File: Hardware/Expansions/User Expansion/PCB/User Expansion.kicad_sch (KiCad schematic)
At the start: 44 parts, among them J101 10018784-10201TLF, U101 M24C02-FMN

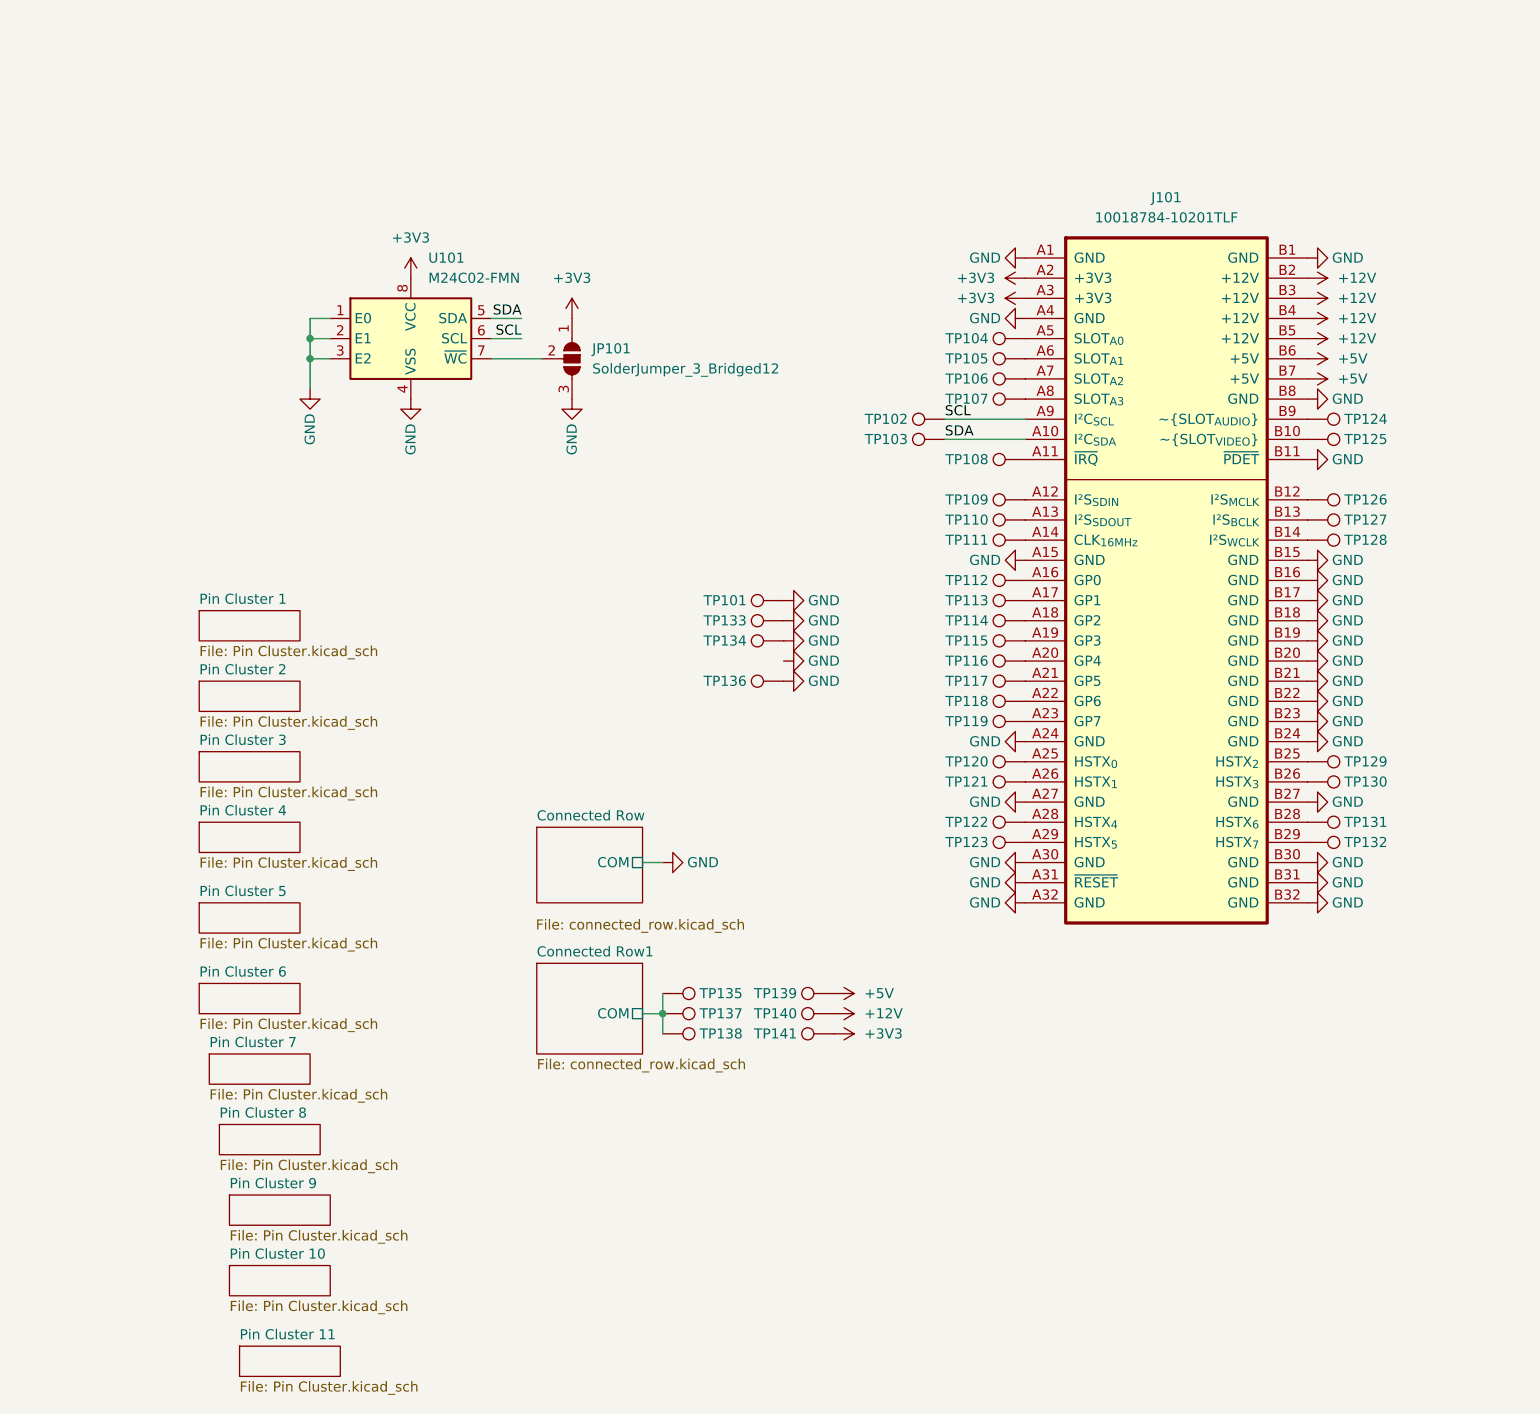
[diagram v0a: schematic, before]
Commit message: Overhauls user expansion and updates design to new platform decisions.
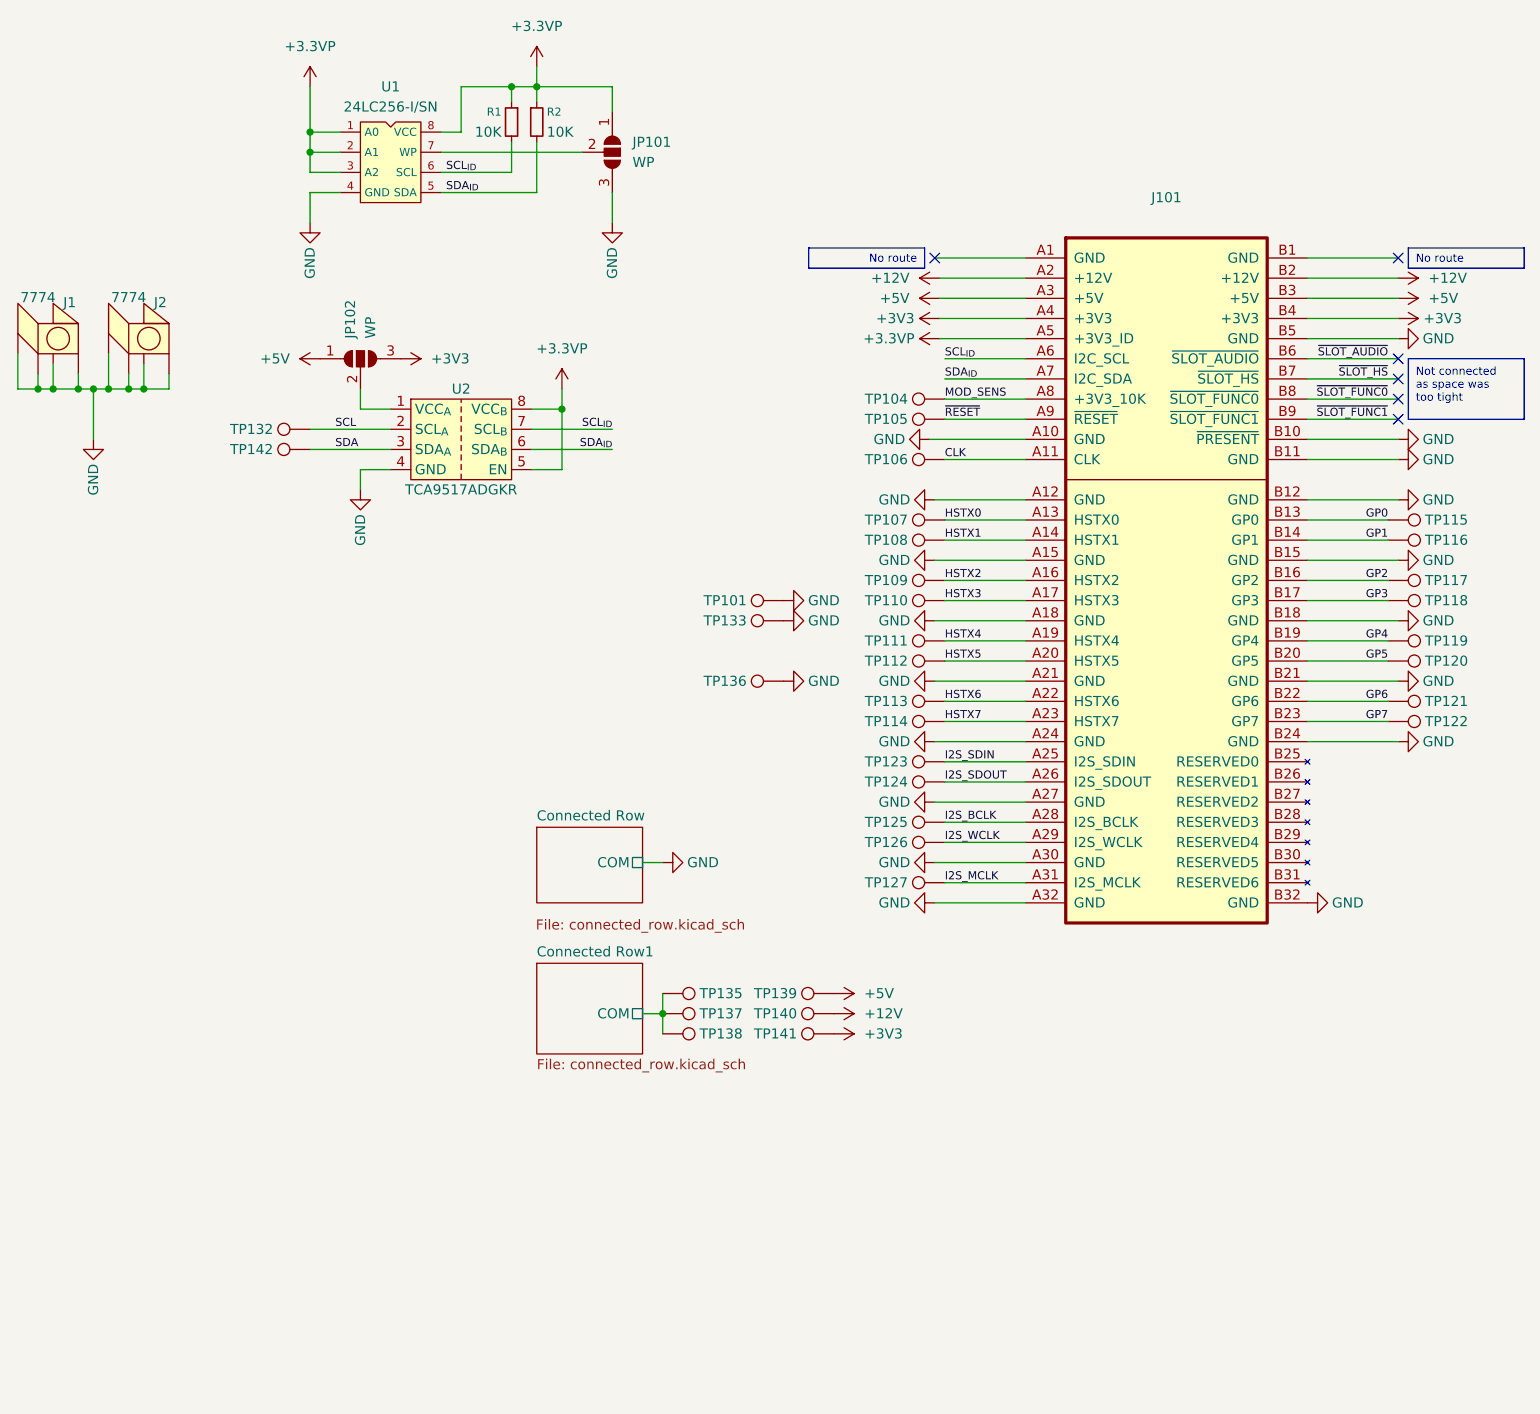
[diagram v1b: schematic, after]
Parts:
- removed TP102: SCL, TestPoint:TestPoint_THTPad_D1.5mm_Drill0.7mm, symbol Connector:TestPoint
- removed TP103: SDA, TestPoint:TestPoint_THTPad_D1.5mm_Drill0.7mm, symbol Connector:TestPoint
- removed TP128: WCLK, TestPoint:TestPoint_THTPad_D1.5mm_Drill0.7mm, symbol Connector:TestPoint
- removed TP129: HSTX2, TestPoint:TestPoint_THTPad_D1.5mm_Drill0.7mm, symbol Connector:TestPoint
- removed TP130: HSTX3, TestPoint:TestPoint_THTPad_D1.5mm_Drill0.7mm, symbol Connector:TestPoint
- removed TP131: HSTX6, TestPoint:TestPoint_THTPad_D1.5mm_Drill0.7mm, symbol Connector:TestPoint
- removed TP134: GP7, TestPoint:TestPoint_THTPad_D1.5mm_Drill0.7mm, symbol Connector:TestPoint
- removed U101: M24C02-FMN, Package_SO:SOIC-8_3.9x4.9mm_P1.27mm, symbol Memory_EEPROM:M24C02-FMN
- added J1, J2: 7774, Home Computer:KEYSTONE_7774, symbol Home Computer:7774
- added JP102: WP, Jumper:SolderJumper-3_P1.3mm_Open_RoundedPad1.0x1.5mm, symbol Jumper:SolderJumper_3_Open
- added R1, R2: 10K, Resistor_SMD:R_0805_2012Metric_Pad1.20x1.40mm_HandSolder, symbol Device:R_Small
- added TP142: (no value), Home Computer:Perfboard_Pad_P2.54mm, symbol Connector:TestPoint
- added U1: 24LC256-I/SN, Package_SO:SOIC-8_3.9x4.9mm_P1.27mm, symbol Home Computer:24LC256
- added U2: TCA9517ADGKR, Package_SO:VSSOP-8_3x3mm_P0.65mm, symbol Home Computer:TCA9517ADGKR
- J101: value 10018784-10201TLF -> (none); symbol Home Computer:AHC-MODCONN-GEN1 Socket -> Home Computer:AHC-CONN-EXP-CARD; MANUFACTURER AMPHENOL -> (none); PARTREV A -> (none); STANDARD MANUFACTURER RECOMMENDATIONS -> (none)
- JP101: value SolderJumper_3_Bridged12 -> WP
- TP101, TP119, TP133, TP135, TP136, TP137, TP138, TP139, TP140, TP141: value GP7 -> (none); footprint TestPoint:TestPoint_THTPad_D1.5mm_Drill0.7mm -> Home Computer:Perfboard_Pad_P2.54mm
- TP104: value A0 -> (none); footprint TestPoint:TestPoint_THTPad_D1.5mm_Drill0.7mm -> Home Computer:Perfboard_Pad_P2.54mm
- TP105: value A1 -> (none); footprint TestPoint:TestPoint_THTPad_D1.5mm_Drill0.7mm -> Home Computer:Perfboard_Pad_P2.54mm
- TP106: value A2 -> (none); footprint TestPoint:TestPoint_THTPad_D1.5mm_Drill0.7mm -> Home Computer:Perfboard_Pad_P2.54mm
- TP107: value A3 -> (none); footprint TestPoint:TestPoint_THTPad_D1.5mm_Drill0.7mm -> Home Computer:Perfboard_Pad_P2.54mm
- TP108: value IRQ -> (none); footprint TestPoint:TestPoint_THTPad_D1.5mm_Drill0.7mm -> Home Computer:Perfboard_Pad_P2.54mm
- TP109: value SDIN -> (none); footprint TestPoint:TestPoint_THTPad_D1.5mm_Drill0.7mm -> Home Computer:Perfboard_Pad_P2.54mm
- TP110: value SDOUT -> (none); footprint TestPoint:TestPoint_THTPad_D1.5mm_Drill0.7mm -> Home Computer:Perfboard_Pad_P2.54mm
- TP111: value 16MHz -> (none); footprint TestPoint:TestPoint_THTPad_D1.5mm_Drill0.7mm -> Home Computer:Perfboard_Pad_P2.54mm
- TP112: value GP0 -> (none); footprint TestPoint:TestPoint_THTPad_D1.5mm_Drill0.7mm -> Home Computer:Perfboard_Pad_P2.54mm
- TP113: value GP1 -> (none); footprint TestPoint:TestPoint_THTPad_D1.5mm_Drill0.7mm -> Home Computer:Perfboard_Pad_P2.54mm
- TP114: value GP2 -> (none); footprint TestPoint:TestPoint_THTPad_D1.5mm_Drill0.7mm -> Home Computer:Perfboard_Pad_P2.54mm
- TP115: value GP3 -> (none); footprint TestPoint:TestPoint_THTPad_D1.5mm_Drill0.7mm -> Home Computer:Perfboard_Pad_P2.54mm
- TP116: value GP4 -> (none); footprint TestPoint:TestPoint_THTPad_D1.5mm_Drill0.7mm -> Home Computer:Perfboard_Pad_P2.54mm
- TP117: value GP5 -> (none); footprint TestPoint:TestPoint_THTPad_D1.5mm_Drill0.7mm -> Home Computer:Perfboard_Pad_P2.54mm
- TP118: value GP6 -> (none); footprint TestPoint:TestPoint_THTPad_D1.5mm_Drill0.7mm -> Home Computer:Perfboard_Pad_P2.54mm
- TP120: value HSTX0 -> (none); footprint TestPoint:TestPoint_THTPad_D1.5mm_Drill0.7mm -> Home Computer:Perfboard_Pad_P2.54mm
- TP121: value HSTX1 -> (none); footprint TestPoint:TestPoint_THTPad_D1.5mm_Drill0.7mm -> Home Computer:Perfboard_Pad_P2.54mm
- TP122: value HSTX4 -> (none); footprint TestPoint:TestPoint_THTPad_D1.5mm_Drill0.7mm -> Home Computer:Perfboard_Pad_P2.54mm
- TP123: value HSTX5 -> (none); footprint TestPoint:TestPoint_THTPad_D1.5mm_Drill0.7mm -> Home Computer:Perfboard_Pad_P2.54mm
- TP124: value ~{AUDIO} -> (none); footprint TestPoint:TestPoint_THTPad_D1.5mm_Drill0.7mm -> Home Computer:Perfboard_Pad_P2.54mm
- TP125: value ~{VIDEO} -> (none); footprint TestPoint:TestPoint_THTPad_D1.5mm_Drill0.7mm -> Home Computer:Perfboard_Pad_P2.54mm
- TP126: value MCLK -> (none); footprint TestPoint:TestPoint_THTPad_D1.5mm_Drill0.7mm -> Home Computer:Perfboard_Pad_P2.54mm
- TP127: value BCLK -> (none); footprint TestPoint:TestPoint_THTPad_D1.5mm_Drill0.7mm -> Home Computer:Perfboard_Pad_P2.54mm
- TP132: value HSTX7 -> (none); footprint TestPoint:TestPoint_THTPad_D1.5mm_Drill0.7mm -> Home Computer:Perfboard_Pad_P2.54mm
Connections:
- net +12V: now also J101.A2 (+12V); no longer J101.B3 (+12V), J101.B4 (+12V), J101.B5 (+12V)
- net +3V3: now also J101.A4 (+3V3), J101.B4 (+3V3), JP102.3 (B); no longer J101.A2 (+3V3), J101.A3 (+3V3), JP101.1 (A)
- net +5V: now also J101.A3 (+5V), J101.B3 (+5V), JP102.1 (A); no longer J101.B6 (+5V), J101.B7 (+5V)
- net GND: now also J101.A10 (GND), J101.A12 (GND), J101.A18 (GND), J101.A21 (GND), J101.B10 (~{PRESENT}), J101.B12 (GND), J101.B5 (GND), J1.1_1, J1.1_2, J1.1_3, J1.1_4, J2.1_1, J2.1_2, J2.1_3, J2.1_4, U1.4 (GND), U2.4 (GND); no longer J101.A1 (GND), J101.A31 (~{RESET}), J101.A4 (GND), J101.B1 (GND), J101.B16 (GND), J101.B17 (GND), J101.B19 (GND), J101.B20 (GND), J101.B22 (GND), J101.B23 (GND), J101.B27 (GND), J101.B30 (GND), J101.B31 (GND), J101.B8 (GND)
- net SCL: now also TP132.1, U2.2 (SCL_{A}); no longer J101.A9 (I²C_{SCL})
- net SDA: now also TP142.1, U2.3 (SDA_{A}); no longer J101.A10 (I²C_{SDA})
- net HSTX2: now reaches TP109.1
- net HSTX2: now also J101.A16 (HSTX2); no longer J101.A12 (I²S_{SDIN})
- net GP7: now reaches TP122.1
- net GP7: now also J101.B23 (GP7); no longer J101.A28 (HSTX_{4})
- net CLK: now reaches J101.A11 (CLK)
- net CLK: now also TP106.1; no longer TP108.1
- net HSTX3: now reaches J101.A17 (HSTX3)
- net HSTX3: now also TP110.1; no longer TP113.1
- net I2S_SDIN: now reaches TP123.1
- net I2S_SDIN: now also J101.A25 (I2S_SDIN); no longer J101.A29 (HSTX_{5})
- net +3.3VP: now reaches J101.A5 (+3V3_ID)
- net +3.3VP: now also JP101.1 (A), R1.1, R2.1, U1.1 (A0), U1.2 (A1), U1.3 (A2), U1.8 (VCC), U2.5 (EN), U2.8 (VCC_{B}); no longer TP104.1
- net HSTX1: now reaches J101.A14 (HSTX1)
- net HSTX1: now also TP108.1; no longer TP111.1
- net GP0: now reaches J101.B13 (GP0)
- net GP0: now also TP115.1; no longer TP127.1
- net GP5: now reaches TP120.1
- net GP5: now also J101.B20 (GP5); no longer J101.A25 (HSTX_{0})
- net HSTX5: now reaches TP112.1
- net HSTX5: now also J101.A20 (HSTX5); no longer J101.A16 (GP0)
- net at JP101.2 (C): now also U1.7 (WP)
- net SDA_{ID}: now reaches J101.A7 (I2C_SDA)
- net SDA_{ID}: now also R2.2, U1.5 (SDA), U2.6 (SDA_{B}); no longer TP106.1
- net HSTX0: now reaches J101.A13 (HSTX0)
- net HSTX0: now also TP107.1; no longer TP110.1
- net HSTX7: now reaches TP114.1
- net HSTX7: now also J101.A23 (HSTX7); no longer J101.A18 (GP2)
- net HSTX4: now reaches J101.A19 (HSTX4)
- net HSTX4: now also TP111.1; no longer TP115.1
- net GP1: now reaches TP116.1
- net GP1: now also J101.B14 (GP1); no longer J101.A20 (GP4)
- net GP2: now reaches TP117.1
- net GP2: now also J101.B16 (GP2); no longer J101.A21 (GP5)
- net GP3: now reaches TP118.1
- net GP3: now also J101.B17 (GP3); no longer J101.A22 (GP6)
- net GP4: now reaches TP119.1
- net GP4: now also J101.B19 (GP4); no longer J101.A23 (GP7)
- net GP6: now reaches TP121.1
- net GP6: now also J101.B22 (GP6); no longer J101.A26 (HSTX_{1})
- net SCL_{ID}: now reaches J101.A6 (I2C_SCL)
- net SCL_{ID}: now also R1.2, U1.6 (SCL), U2.7 (SCL_{B}); no longer TP105.1
- net MOD_SENS: now reaches J101.A8 (+3V3_10K)
- net MOD_SENS: now also TP104.1; no longer TP107.1
- net I2S_BCLK: now reaches TP125.1
- net I2S_BCLK: now also J101.A28 (I2S_BCLK); no longer J101.B10 (~{SLOT_{VIDEO}})
- net I2S_WCLK: now reaches TP126.1
- net I2S_WCLK: now also J101.A29 (I2S_WCLK); no longer J101.B12 (I²S_{MCLK})
- net at J101.B29 (RESERVED4): no longer TP132.1
- net I2S_SDOUT: now reaches TP124.1
- net I2S_SDOUT: now also J101.A26 (I2S_SDOUT); no longer J101.B9 (~{SLOT_{AUDIO}})
- new net: JP102.2 (C), U2.1 (VCC_{A})
- new net HSTX6: J101.A22 (HSTX6), TP113.1
- new net I2S_MCLK: J101.A31 (I2S_MCLK), TP127.1
- new net ~{RESET}: J101.A9 (~{RESET}), TP105.1
- new net ~{SLOT_AUDIO}: J101.B6 (~{SLOT_AUDIO})
- new net ~{SLOT_FUNC0}: J101.B8 (~{SLOT_FUNC0})
- new net ~{SLOT_FUNC1}: J101.B9 (~{SLOT_FUNC1})
- new net ~{SLOT_HS}: J101.B7 (~{SLOT_HS})
- no-connect marks 0 -> 6
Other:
- removed sheet Pin Cluster 1
- removed sheet Pin Cluster 10
- removed sheet Pin Cluster 11
- removed sheet Pin Cluster 2
- removed sheet Pin Cluster 3
- removed sheet Pin Cluster 4
- removed sheet Pin Cluster 5
- removed sheet Pin Cluster 6
- removed sheet Pin Cluster 7
- removed sheet Pin Cluster 8
- removed sheet Pin Cluster 9
- moved on the sheet: JP101
